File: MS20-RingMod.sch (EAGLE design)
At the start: 28 parts, among them IC1 TL072P, IC2 4030N, IC3 TL084P, U1 POWER

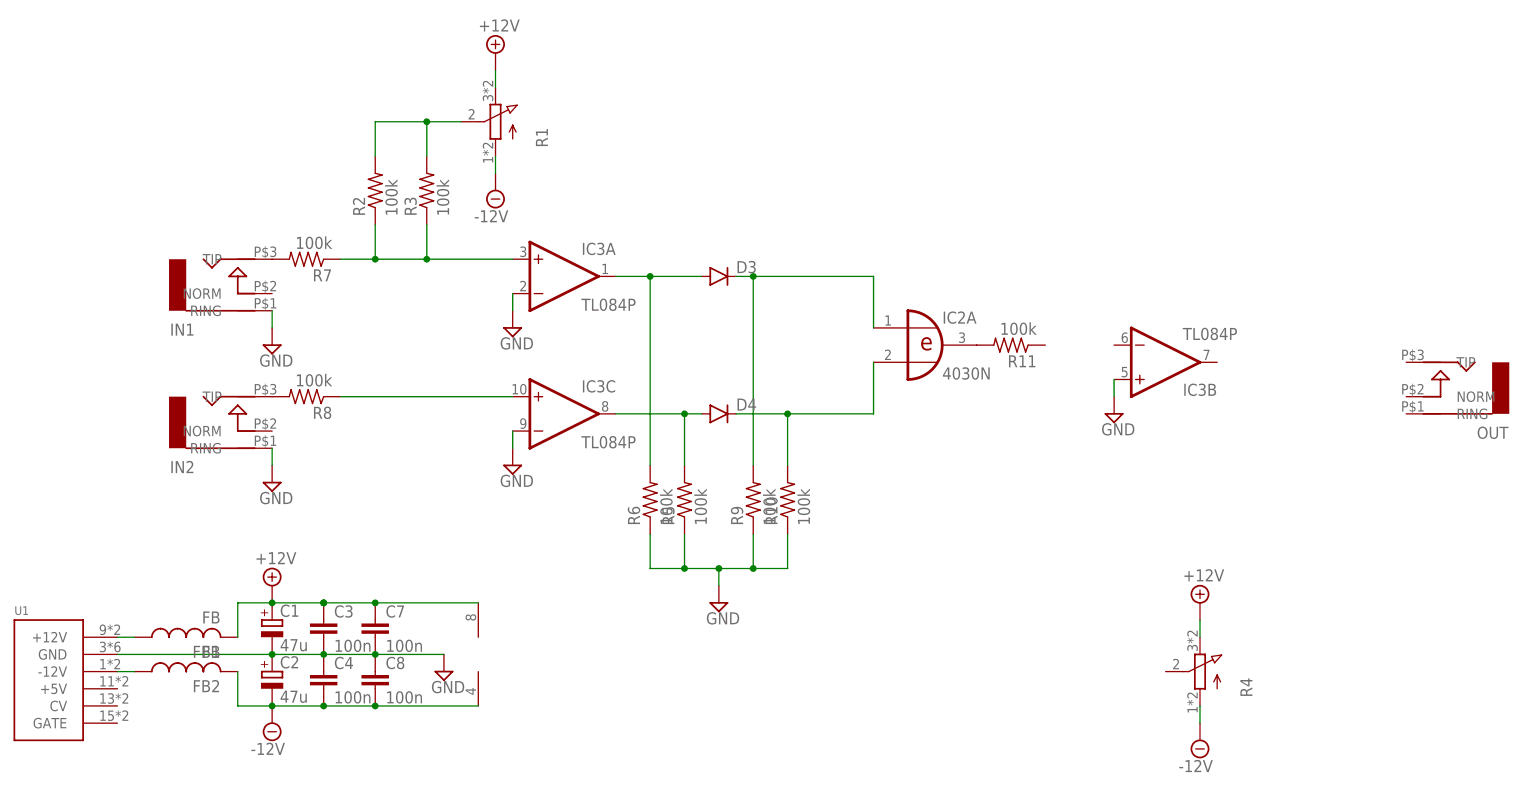
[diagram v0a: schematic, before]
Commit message: a schemo with discrete xor
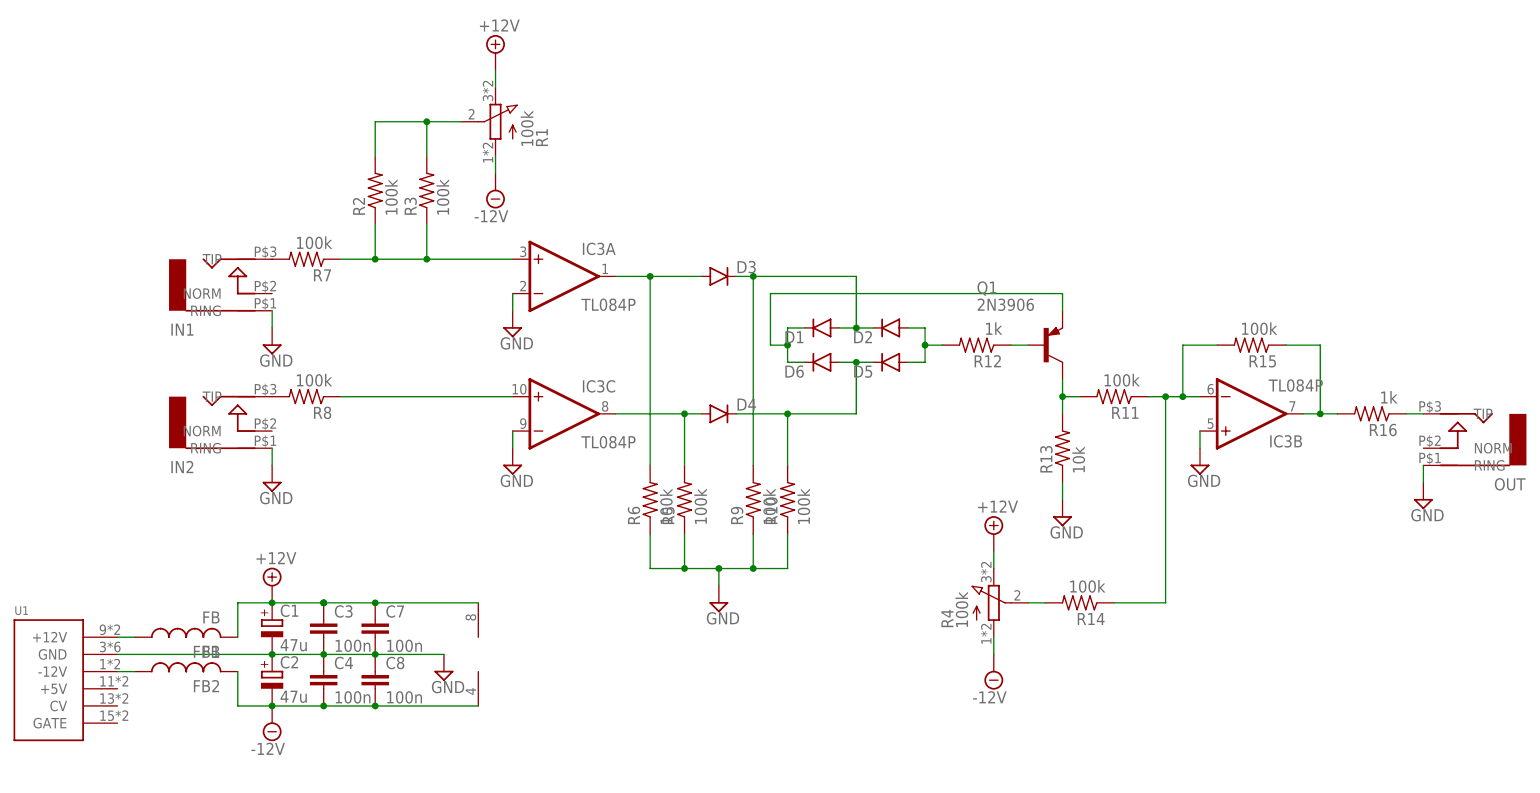
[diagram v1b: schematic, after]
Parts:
- removed IC2: 4030N, 40xx:4030N
- added D1, D2, D5, D6: (no value), SparkFun-DiscreteSemi:DIODE1N4148
- added Q1: 2N3906, transistor-pnp:2N3906
- added R12, R16: 1k, rcl:R-US_0207/7
- added R13: 10k, rcl:R-US_0207/7
- added R14, R15: 100k, rcl:R-US_0207/7
- R1, R4: value (none) -> 100k
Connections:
- new net N$13: D2.A, D5.A, R12.2
- new net N$14: Q1.B, R12.1
- new net N$15: R14.2, R4.S
- new net N$16: IC3B.OUT, R15.1, R16.2
- new net N$17: OUT.TIP, R16.1
- new net N$18: IC3B.-IN, R11.1, R14.1, R15.2
- new net N$3: Q1.C, R11.2, R13.2
- net GND: now also OUT.RING, R13.1
- net N$10: now also D5.C, D6.A; no longer IC2A.I1
- net N$12: now also D1.C, D6.C, Q1.E; no longer IC2A.O, R11.2
- net N$9: now also D1.A, D2.C; no longer IC2A.I0
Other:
- moved on the sheet: IC3B, OUT, R11, R4

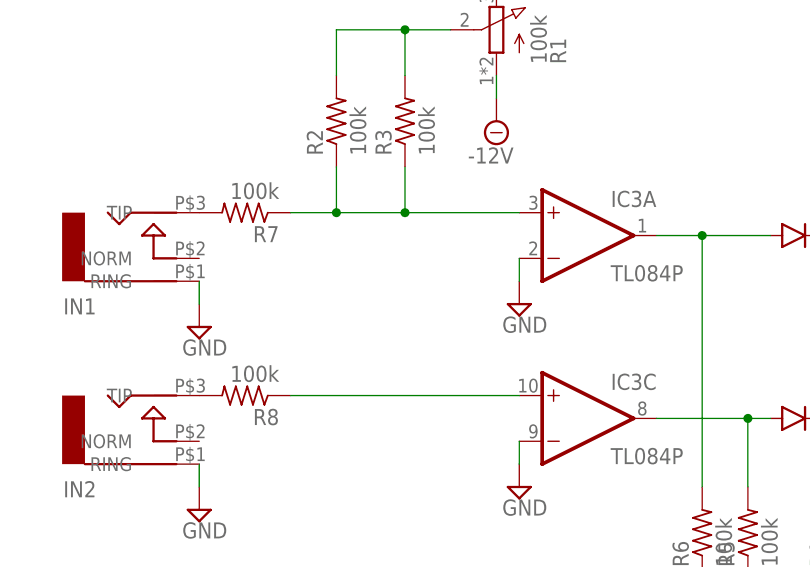
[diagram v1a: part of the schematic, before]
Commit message: fixed input pullup thing
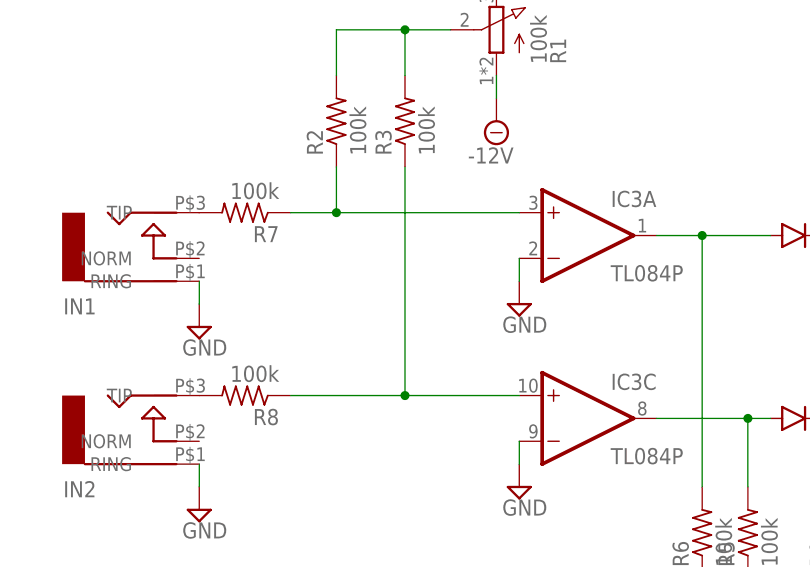
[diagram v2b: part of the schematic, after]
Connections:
- net N$6: now also R3.1
- net N$7: no longer R3.1
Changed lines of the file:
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@@
 <?xml version="1.0" encoding="utf-8"?>
 <!DOCTYPE eagle SYSTEM "eagle.dtd">
-<eagle version="7.6.0">
+<eagle version="8.3.2">
 <drawing>
 <settings>
 <setting alwaysvectorfont="no"/>
+<setting keepoldvectorfont="yes"/>
 <setting verticaltext="up"/>
 </settings>
 <grid distance="0.1" unitdist="inch" unit="inch" style="lines" multiple="1" display="no" altdistance="0.01" altunitdist="inch" altunit="inch"/>
 <layers>
-<layer number="1" name="Top" color="4" fill="1" visible="yes" active="no"/>
-<layer number="16" name="Bottom" color="1" fill="1" visible="yes" active="no"/>
-<layer number="17" name="Pads" color="2" fill="1" visible="yes" active="no"/>
-<layer number="18" name="Vias" color="2" fill="1" visible="yes" active="no"/>
-<layer number="19" name="Unrouted" color="6" fill="1" visible="yes" active="no"/>
-<layer number="20" name="Dimension" color="15" fill="1" visible="yes" active="no"/>
-<layer number="21" name="tPlace" color="7" fill="1" visible="yes" active="no"/>
-<layer number="22" name="bPlace" color="7" fill="1" visible="yes" active="no"/>
-<layer number="23" name="tOrigins" color="15" fill="1" visible="yes" active="no"/>
-<layer number="24" name="bOrigins" color="15" fill="1" visible="yes" active="no"/>
-<layer number="25" name="tNames" color="7" fill="1" visible="yes" active="no"/>
-<layer number="26" name="bNames" color="7" fill="1" visible="yes" active="no"/>
-<layer number="27" name="tValues" color="7" fill="1" visible="yes" active="no"/>
-<layer number="28" name="bValues" color="7" fill="1" visible="yes" active="no"/>
+<layer number="1" name="Top" color="4" fill="1" visible="no" active="no"/>
+<layer number="16" name="Bottom" color="1" fill="1" visible="no" active="no"/>
+<layer number="17" name="Pads" color="2" fill="1" visible="no" active="no"/>
+<layer number="18" name="Vias" color="2" fill="1" visible="no" active="no"/>
+<layer number="19" name="Unrouted" color="6" fill="1" visible="no" active="no"/>
+<layer number="20" name="Dimension" color="15" fill="1" visible="no" active="no"/>
+<layer number="21" name="tPlace" color="7" fill="1" visible="no" active="no"/>
+<layer number="22" name="bPlace" color="7" fill="1" visible="no" active="no"/>
+<layer number="23" name="tOrigins" color="15" fill="1" visible="no" active="no"/>
+<layer number="24" name="bOrigins" color="15" fill="1" visible="no" active="no"/>
+<layer number="25" name="tNames" color="7" fill="1" visible="no" active="no"/>
+<layer number="26" name="bNames" color="7" fill="1" visible="no" active="no"/>
+<layer number="27" name="tValues" color="7" fill="1" visible="no" active="no"/>
+<layer number="28" name="bValues" color="7" fill="1" visible="no" active="no"/>
 <layer number="29" name="tStop" color="7" fill="3" visible="no" active="no"/>
 <layer number="30" name="bStop" color="7" fill="6" visible="no" active="no"/>
@@
 <layer number="35" name="tGlue" color="7" fill="4" visible="no" active="no"/>
 <layer number="36" name="bGlue" color="7" fill="5" visible="no" active="no"/>
-<layer number="37" name="tTest" color="7" fill="1" visible="yes" active="no"/>
-<layer number="38" name="bTest" color="7" fill="1" visible="yes" active="no"/>
+<layer number="37" name="tTest" color="7" fill="1" visible="no" active="no"/>
+<layer number="38" name="bTest" color="7" fill="1" visible="no" active="no"/>
 <layer number="39" name="tKeepout" color="4" fill="11" visible="no" active="no"/>
 <layer number="40" name="bKeepout" color="1" fill="11" visible="no" active="no"/>
@@
 <layer number="44" name="Drills" color="7" fill="1" visible="no" active="no"/>
 <layer number="45" name="Holes" color="7" fill="1" visible="no" active="no"/>
-<layer number="46" name="Milling" color="3" fill="1" visible="yes" active="no"/>
-<layer number="47" name="Measures" color="7" fill="1" visible="yes" active="no"/>
-<layer number="48" name="Document" color="7" fill="1" visible="yes" active="no"/>
-<layer number="49" name="Reference" color="7" fill="1" visible="yes" active="no"/>
-<layer number="50" name="dxf" color="7" fill="1" visible="yes" active="no"/>
-<layer number="51" name="tDocu" color="7" fill="1" visible="yes" active="no"/>
-<layer number="52" name="bDocu" color="7" fill="1" visible="yes" active="no"/>
-<layer number="53" name="tGND_GNDA" color="7" fill="9" visible="yes" active="no"/>
-<layer number="54" name="bGND_GNDA" color="1" fill="9" visible="yes" active="no"/>
-<layer number="56" name="wert" color="7" fill="1" visible="yes" active="no"/>
-<layer number="57" name="tCAD" color="7" fill="1" visible="yes" active="no"/>
-<layer number="59" name="tCarbon" color="7" fill="1" visible="yes" active="no"/>
-<layer number="60" name="bCarbon" color="7" fill="1" visible="yes" active="no"/>
+<layer number="46" name="Milling" color="3" fill="1" visible="no" active="no"/>
+<layer number="47" name="Measures" color="7" fill="1" visible="no" active="no"/>
+<layer number="48" name="Document" color="7" fill="1" visible="no" active="no"/>
+<layer number="49" name="Reference" color="7" fill="1" visible="no" active="no"/>
+<layer number="50" name="dxf" color="7" fill="1" visible="no" active="no"/>
+<layer number="51" name="tDocu" color="7" fill="1" visible="no" active="no"/>
+<layer number="52" name="bDocu" color="7" fill="1" visible="no" active="no"/>
+<layer number="53" name="tGND_GNDA" color="7" fill="9" visible="no" active="no"/>
+<layer number="54" name="bGND_GNDA" color="1" fill="9" visible="no" active="no"/>
+<layer number="56" name="wert" color="7" fill="1" visible="no" active="no"/>
+<layer number="57" name="tCAD" color="7" fill="1" visible="no" active="no"/>
+<layer number="59" name="tCarbon" color="7" fill="1" visible="no" active="no"/>
+<layer number="60" name="bCarbon" color="7" fill="1" visible="no" active="no"/>
 <layer number="90" name="Modules" color="5" fill="1" visible="yes" active="yes"/>
 <layer number="91" name="Nets" color="2" fill="1" visible="yes" active="yes"/>
@@
 <pinref part="SUPPLY1" gate="+12V" pin="+12V"/>
 <junction x="86.36" y="20.32"/>
-<pinref part="SUPPLY1" gate="+12V" pin="+12V"/>
 <pinref part="C3" gate="G$1" pin="1"/>
 <wire x1="86.36" y1="20.32" x2="93.98" y2="20.32" width="0.1524" layer="91"/>
@@
 <pinref part="SUPPLY2" gate="G$1" pin="-12V"/>
 <junction x="86.36" y="5.08"/>
-<pinref part="SUPPLY2" gate="G$1" pin="-12V"/>
 <pinref part="C4" gate="G$1" pin="2"/>
 <wire x1="86.36" y1="5.08" x2="93.98" y2="5.08" width="0.1524" layer="91"/>
@@
 <pinref part="R8" gate="G$1" pin="1"/>
 <pinref part="IC3" gate="C" pin="+IN"/>
-<wire x1="96.52" y1="50.8" x2="121.92" y2="50.8" width="0.1524" layer="91"/>
+<wire x1="96.52" y1="50.8" x2="109.22" y2="50.8" width="0.1524" layer="91"/>
+<pinref part="R3" gate="G$1" pin="1"/>
+<wire x1="109.22" y1="50.8" x2="121.92" y2="50.8" width="0.1524" layer="91"/>
+<wire x1="109.22" y1="76.2" x2="109.22" y2="50.8" width="0.1524" layer="91"/>
+<junction x="109.22" y="50.8"/>
 </segment>
 </net>
@@
 <pinref part="IC3" gate="A" pin="+IN"/>
 <pinref part="R7" gate="G$1" pin="1"/>
-<wire x1="121.92" y1="71.12" x2="109.22" y2="71.12" width="0.1524" layer="91"/>
+<wire x1="121.92" y1="71.12" x2="101.6" y2="71.12" width="0.1524" layer="91"/>
 <pinref part="R2" gate="G$1" pin="1"/>
-<wire x1="109.22" y1="71.12" x2="101.6" y2="71.12" width="0.1524" layer="91"/>
 <wire x1="101.6" y1="71.12" x2="96.52" y2="71.12" width="0.1524" layer="91"/>
 <wire x1="101.6" y1="76.2" x2="101.6" y2="71.12" width="0.1524" layer="91"/>
 <junction x="101.6" y="71.12"/>
-<pinref part="R3" gate="G$1" pin="1"/>
-<wire x1="109.22" y1="76.2" x2="109.22" y2="71.12" width="0.1524" layer="91"/>
-<junction x="109.22" y="71.12"/>
-</segment>
-</net>
+</segment>
+</net>
